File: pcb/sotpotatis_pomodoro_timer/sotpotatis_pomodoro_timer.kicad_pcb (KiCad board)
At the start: 2 copper layers, 46 parts, among them J1 GENERIC_PWR_IN, J2 USB_C_PWR_IN, SW1 RIGHT_BTN, SW2 PRESET_1_BTN, SW3 PRESET_2_BTN, SW4 PRESET_3_BTN, SW5 LEFT_BTN, SW6 PWR_SWITCH, U1 ATtiny84A-P

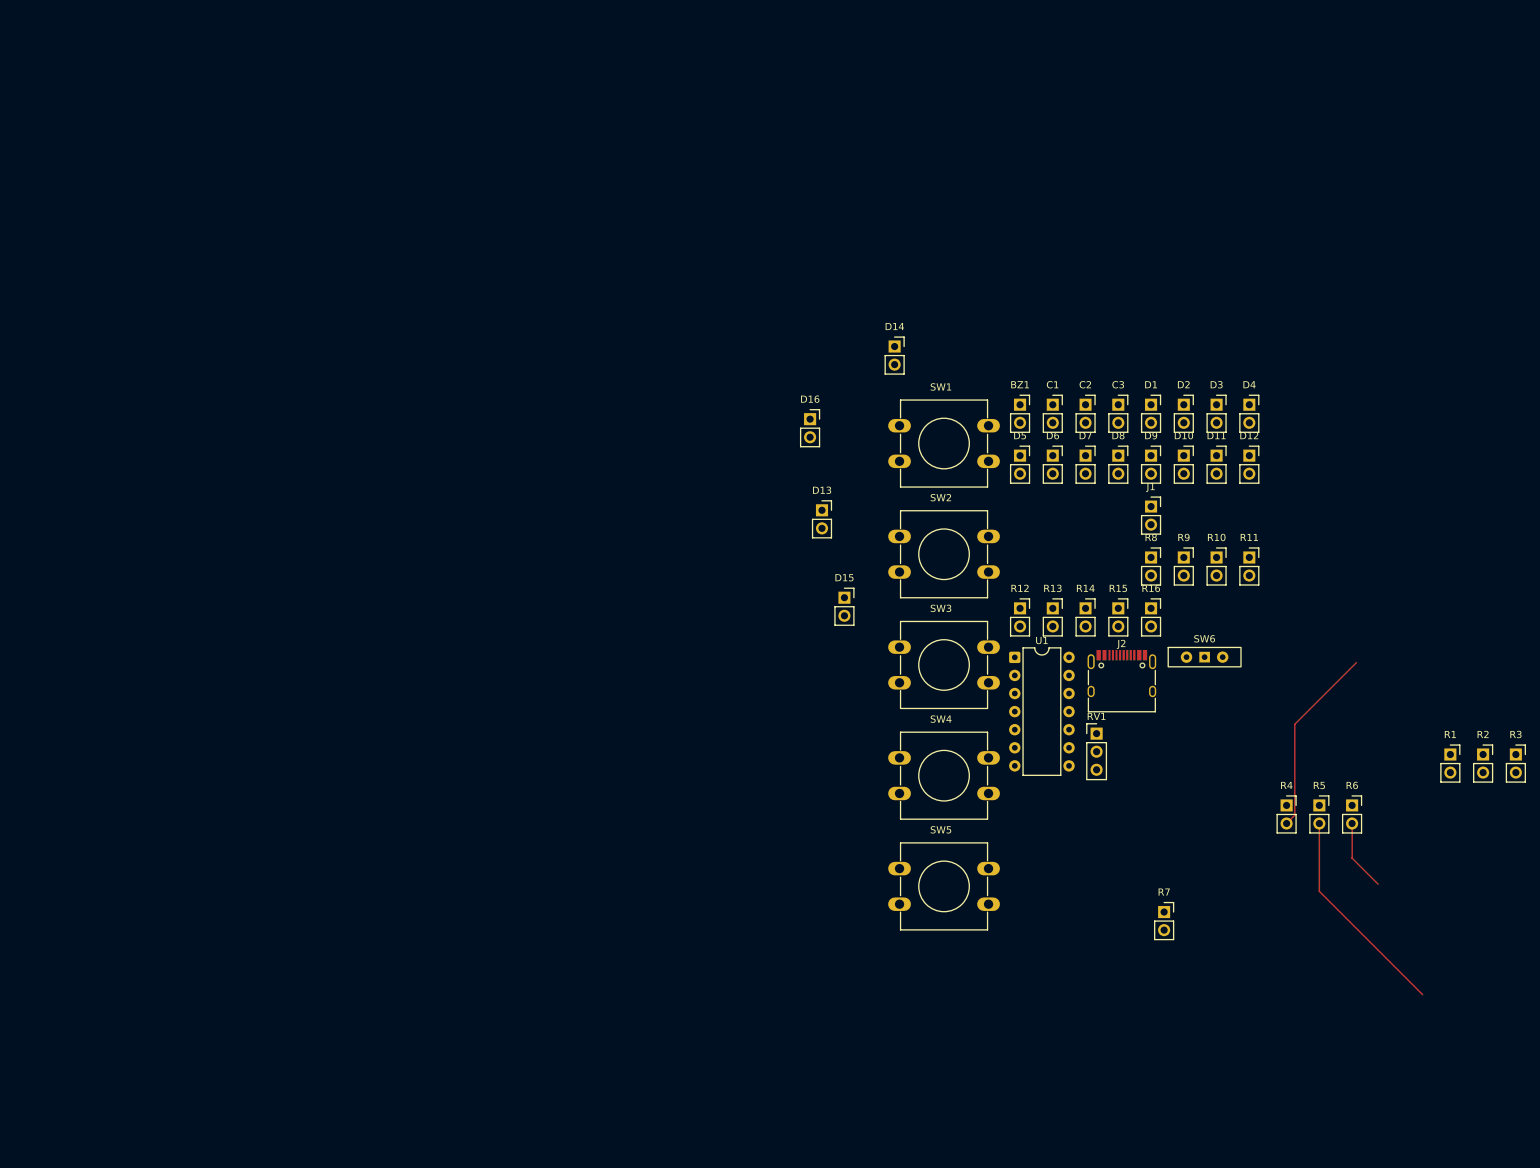
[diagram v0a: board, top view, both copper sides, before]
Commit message: add: Fix footprints in PCB, start setting up DRC settings
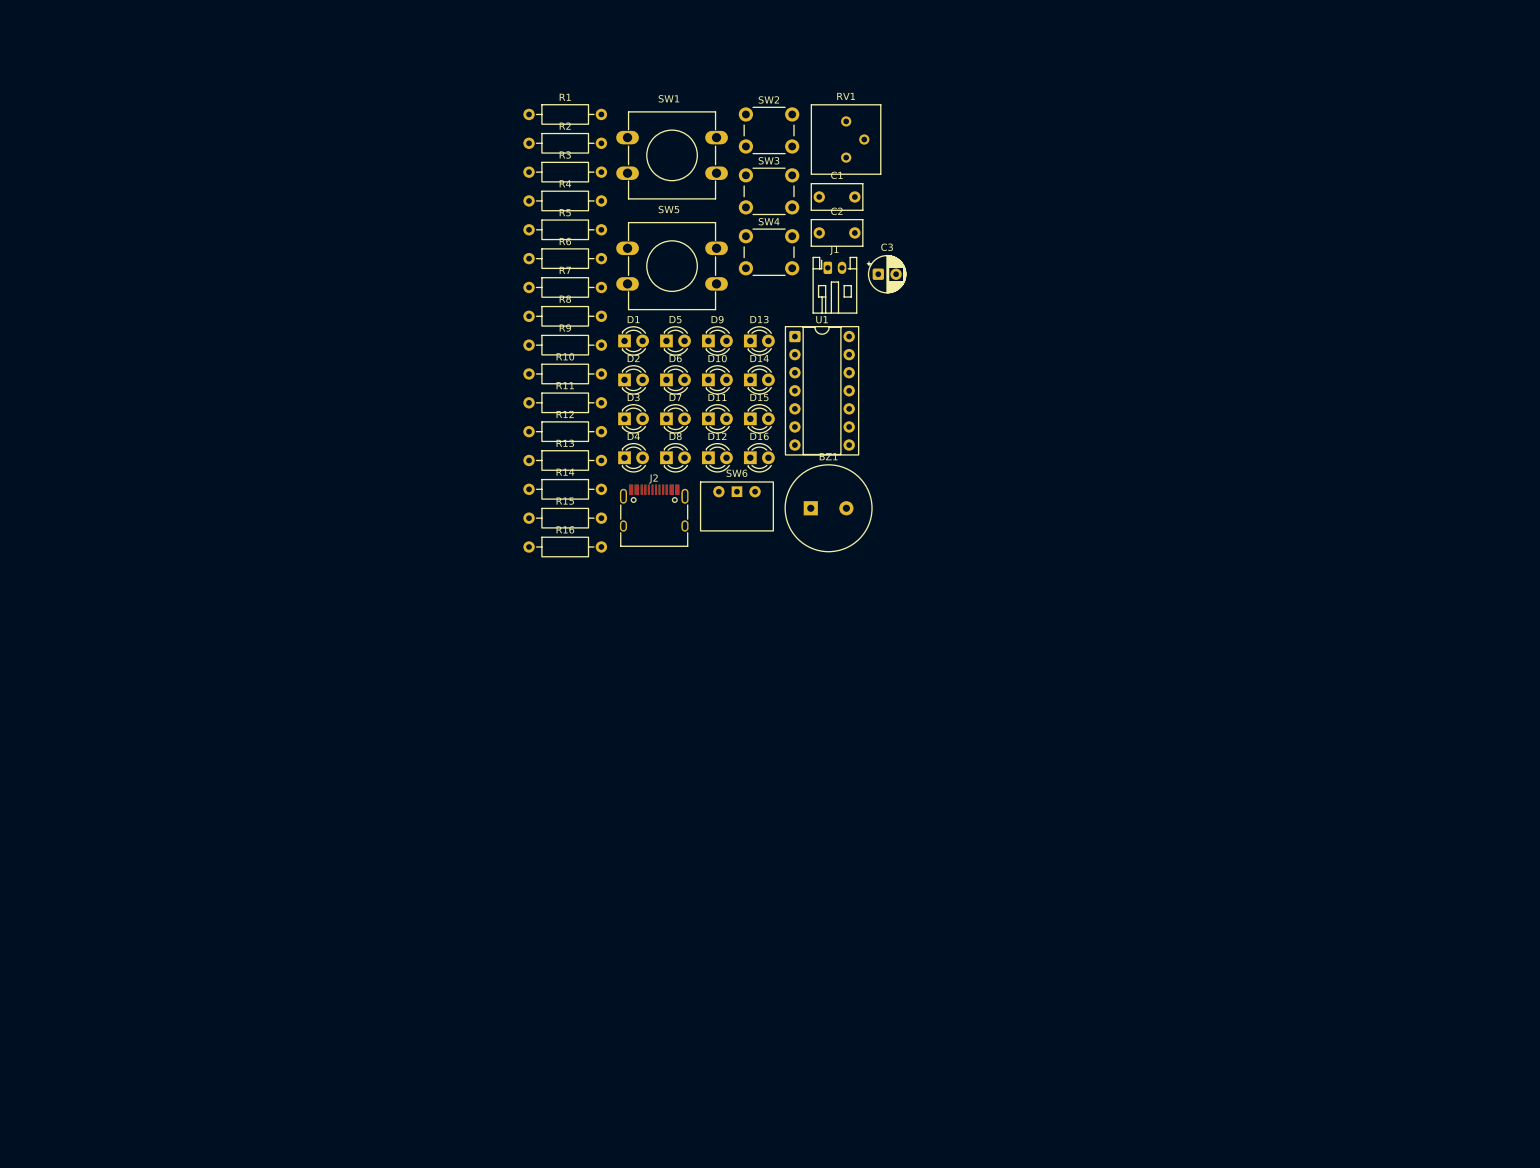
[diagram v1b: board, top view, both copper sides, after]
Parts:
- BZ1: footprint Connector_PinSocket_2.54mm:PinSocket_1x02_P2.54mm_Vertical -> custom-project-libraries:Buzzer_12x5.5RM0.6
- C1, C2: footprint Connector_PinSocket_2.54mm:PinSocket_1x02_P2.54mm_Vertical -> Capacitor_THT:C_Rect_L7.0mm_W3.5mm_P5.00mm
- C3: footprint Connector_PinSocket_2.54mm:PinSocket_1x02_P2.54mm_Vertical -> Capacitor_THT:CP_Radial_D5.0mm_P2.50mm
- D1, D10, D11, D12, D13, D14, D15, D16, D2, D3, D4, D5, D6, D7, D8, D9: footprint Connector_PinSocket_2.54mm:PinSocket_1x02_P2.54mm_Vertical -> LED_THT:LED_D3.0mm
- J1: footprint Connector_PinSocket_2.54mm:PinSocket_1x02_P2.54mm_Vertical -> Connector_JST:JST_PH_S2B-PH-K_1x02_P2.00mm_Horizontal
- R1, R10, R11, R12, R13, R14, R15, R16, R2, R3, R4, R5, R6, R7, R8, R9: footprint Connector_PinSocket_2.54mm:PinSocket_1x02_P2.54mm_Vertical -> Resistor_THT:R_Axial_DIN0207_L6.3mm_D2.5mm_P10.16mm_Horizontal
- RV1: footprint Connector_PinHeader_2.54mm:PinHeader_1x03_P2.54mm_Vertical -> Potentiometer_THT:Potentiometer_Bourns_3386P_Vertical
- SW2, SW3, SW4: footprint Button_Switch_THT:SW_PUSH-12mm -> Button_Switch_THT:SW_PUSH_6mm_H5mm
- SW6: footprint Button_Switch_THT:SW_Slide-03_Wuerth-WS-SLTV_10x2.5x6.4_P2.54mm -> custom-project-libraries:SW_Slide-03_Wuerth-WS-SLTU_10x2.5mm_P2.54mm
- U1: footprint Package_DIP:DIP-14_W7.62mm -> Package_DIP:DIP-14_W7.62mm_Socket
- moved R3 160.9 mm to (84.0, 55.4)
- moved R2 159.1 mm to (84.0, 51.4)
- moved R1 157.6 mm to (84.0, 47.3)
- moved R6 138.8 mm to (84.0, 67.6)
- moved R5 137.3 mm to (84.0, 63.5)
- moved R4 136.1 mm to (84.0, 59.5)
- moved R7 125.1 mm to (84.0, 71.6)
- moved R11 103.5 mm to (84.0, 87.8)
- moved R10 99.9 mm to (84.0, 83.8)
- moved R9 96.7 mm to (84.0, 79.7)
- moved SW5 95.1 mm to (97.8, 66.1)
- moved R8 93.7 mm to (84.0, 75.7)
- moved RV1 88.2 mm to (128.5, 53.4)
- moved D4 88.1 mm to (97.4, 95.5)
- moved R16 87.8 mm to (84.0, 108.1)
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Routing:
- net Net-(D10-A): track 30.0 -> 0.00 mm
- net Net-(D11-A): track 26.6 -> 0.00 mm
- net Net-(D13-K): track 10.0 -> 0.00 mm

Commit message: add: Finalize DRC settings, switch to 4-layer
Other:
- copper layers 2 -> 4
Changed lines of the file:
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@@
 	(generator_version "9.0")
 	(general
-		(thickness 1.6)
+		(thickness 1.586)
 		(legacy_teardrops no)
 	)
@@
 	(layers
 		(0 "F.Cu" signal)
+		(4 "In1.Cu" signal)
+		(6 "In2.Cu" signal)
 		(2 "B.Cu" signal)
 		(9 "F.Adhes" user "F.Adhesive")
@@
 			(layer "F.SilkS"
 				(type "Top Silk Screen")
+				(color "White")
 			)
 			(layer "F.Paste"
@@
 			(layer "F.Mask"
 				(type "Top Solder Mask")
+				(color "Black")
 				(thickness 0.01)
 			)
@@
 			)
 			(layer "dielectric 1"
+				(type "prepreg")
+				(thickness 0.203)
+				(material "FR4")
+				(epsilon_r 4.5)
+				(loss_tangent 0.02)
+			)
+			(layer "In1.Cu"
+				(type "copper")
+				(thickness 0.03)
+			)
+			(layer "dielectric 2"
 				(type "core")
-				(thickness 1.51)
+				(thickness 1.03)
+				(material "FR4")
+				(epsilon_r 4.5)
+				(loss_tangent 0.02)
+			)
+			(layer "In2.Cu"
+				(type "copper")
+				(thickness 0.03)
+			)
+			(layer "dielectric 3"
+				(type "prepreg")
+				(thickness 0.203)
 				(material "FR4")
 				(epsilon_r 4.5)
@@
 			(layer "B.Mask"
 				(type "Bottom Solder Mask")
+				(color "Black")
 				(thickness 0.01)
 			)
@@
 			(layer "B.SilkS"
 				(type "Bottom Silk Screen")
+				(color "White")
 			)
 			(copper_finish "None")
@@
 		)
 	)
+	(segment
+		(start 113.154 100.286)
+		(end 113.154 100.2)
+		(width 0.2)
+		(layer "F.Cu")
+		(net 11)
+	)
+	(segment
+		(start 113.154 100.2)
+		(end 113.03 100.076)
+		(width 0.2)
+		(layer "F.Cu")
+		(net 11)
+	)
 	(embedded_fonts no)

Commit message: add: Backup PCB progress. Working with placement.
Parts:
- C1, C2: footprint Capacitor_THT:C_Rect_L7.0mm_W3.5mm_P5.00mm -> Capacitor_SMD:C_1206_3216Metric_Pad1.33x1.80mm_HandSolder
- C3: footprint Capacitor_THT:CP_Radial_D5.0mm_P2.50mm -> Capacitor_SMD:C_1206_3216Metric_Pad1.33x1.80mm_HandSolder; moved to B.Cu
- D16, J1, J2, SW6: moved to B.Cu
- R1, R10, R11, R12, R2, R3, R4, R5, R6, R7, R8, R9: footprint Resistor_THT:R_Axial_DIN0207_L6.3mm_D2.5mm_P10.16mm_Horizontal -> Resistor_SMD:R_0805_2012Metric_Pad1.20x1.40mm_HandSolder
- R13: value 2.2K -> 2.2k; footprint Resistor_THT:R_Axial_DIN0207_L6.3mm_D2.5mm_P10.16mm_Horizontal -> Resistor_SMD:R_0805_2012Metric_Pad1.20x1.40mm_HandSolder; moved to B.Cu
- R14, R15, R16: footprint Resistor_THT:R_Axial_DIN0207_L6.3mm_D2.5mm_P10.16mm_Horizontal -> Resistor_SMD:R_0805_2012Metric_Pad1.20x1.40mm_HandSolder; moved to B.Cu
- SW1, SW5: footprint Button_Switch_THT:SW_PUSH-12mm -> Button_Switch_THT:SW_PUSH_6mm_H5mm
- moved R2 117.4 mm to (139.8, 154.6), turned to 90 degrees
- moved R5 117.2 mm to (157.2, 155.0), turned to 90 degrees
- moved R1 117.0 mm to (132.6, 153.7), turned to 90 degrees
- moved R3 115.8 mm to (143.8, 154.5), turned to 90 degrees
- moved R8 111.8 mm to (179.2, 134.2), turned to 90 degrees
- moved SW1 110.3 mm to (170.2, 133.8)
- moved R13 109.0 mm to (179.3, 148.7), turned to 180 degrees
- moved R6 108.6 mm to (161.1, 144.0), turned to 90 degrees
- moved R14 108.4 mm to (178.5, 153.0), turned to 90 degrees
- moved R4 107.7 mm to (136.1, 153.7), turned to 90 degrees
- moved R16 106.5 mm to (178.5, 157.2), turned to 90 degrees
- moved R9 99.9 mm to (167.8, 134.0), turned to 90 degrees
- moved SW2 97.0 mm to (158.7, 133.6)
- moved R15 95.1 mm to (165.5, 153.0), turned to 90 degrees
- moved J1 93.5 mm to (163.8, 154.3), turned to 180 degrees
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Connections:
- C3 pad 1: VCC -> +5V
- J1 pad 2: Net-(J1-Pin_2) -> +5V
- J2 pad A4: Net-(J1-Pin_2) -> +5V
- J2 pad A9: Net-(J1-Pin_2) -> +5V
- J2 pad B4: Net-(J1-Pin_2) -> +5V
- J2 pad B9: Net-(J1-Pin_2) -> +5V
- SW6 pad 1: Net-(J1-Pin_2) -> +5V
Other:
- board outline added: 88 x 62.7 mm
- board text added: "1"
- board text added: "10M"
- board text added: "15M"
- board text added: "1M"
- board text added: "20M"
- board text added: "25M"
- board text added: "30M"
- board text added: "3M"
- board text added: "45M"
- board text added: "5M"
- board text added: "60M"
- board text added: "75M"
- board text added: "90M"
- board text added: "BREAK"
- board text added: "PRESETS"
- board text added: "PUT ICONS HERE AND NEWLINES?"
- board text added: "REPETITIONS"
- board text added: "VOLUME"
- board text added: "WORK"

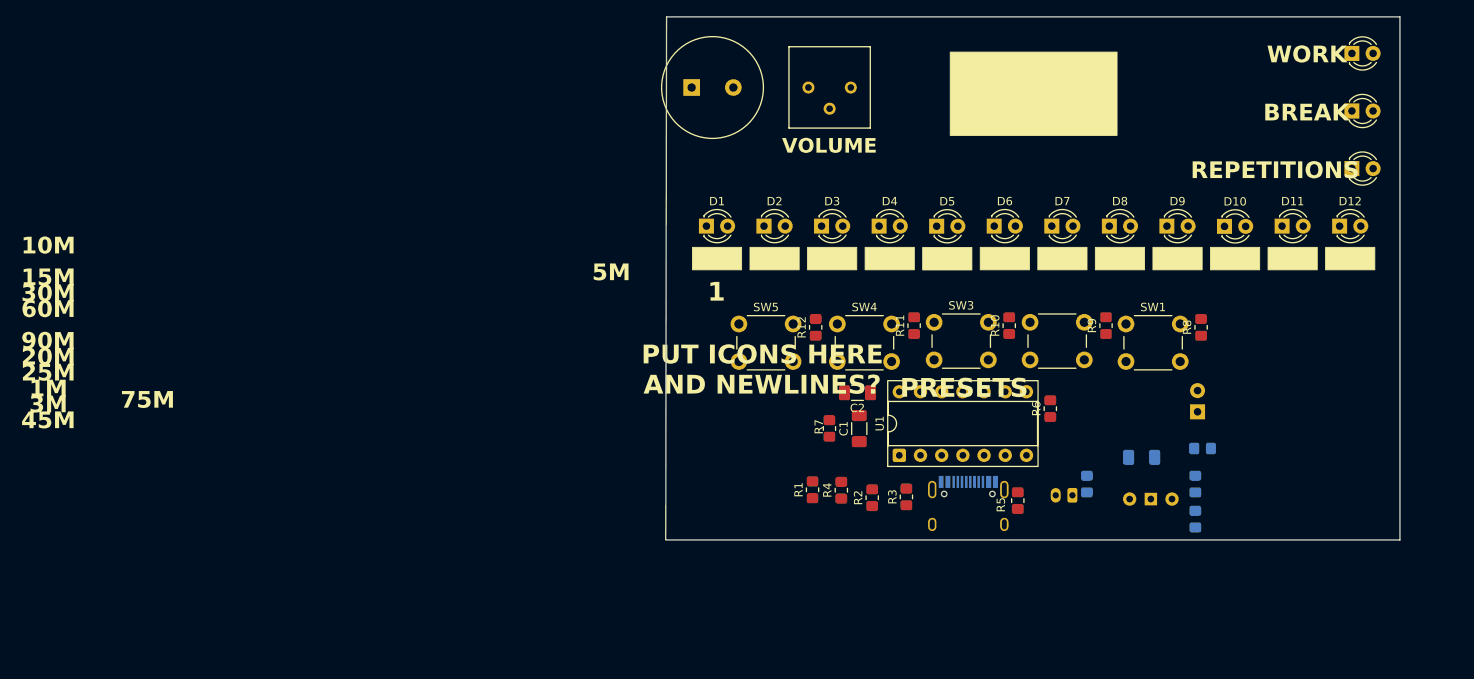
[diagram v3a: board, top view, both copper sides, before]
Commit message: add: Layout variant 1 of PCB
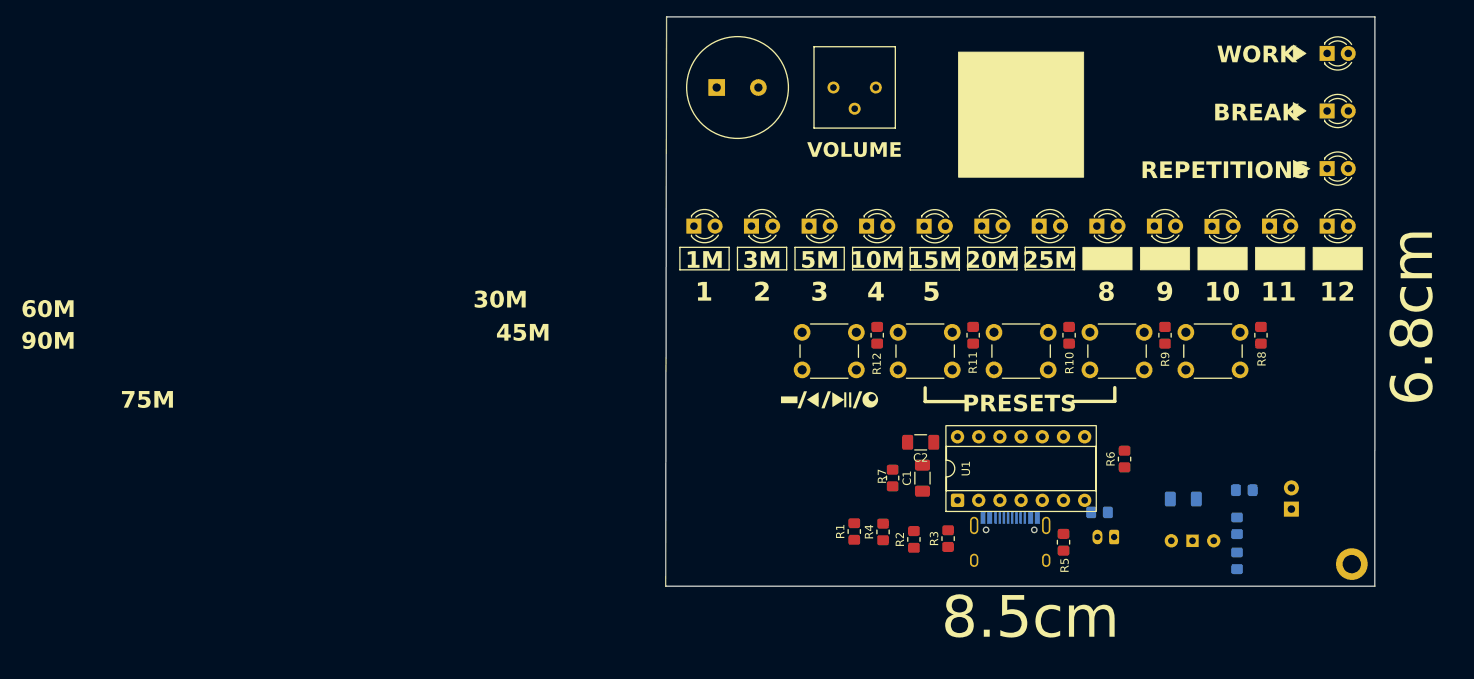
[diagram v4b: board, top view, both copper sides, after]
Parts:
- added G***: LOGO, LOGO, F.Cu at (134.6, 142.9)
- added REF**: MountingHole_2.2mm_M2_DIN965_Pad, MountingHole:MountingHole_2.2mm_M2_DIN965_Pad, F.Cu at (197.2, 162.6)
- moved D16 16.2 mm to (190.0, 156.0)
- moved R6 10.8 mm to (170.0, 150.0)
- moved C1 9.62 mm to (145.8, 152.3)
- moved R7 9.62 mm to (142.2, 152.3)
- moved C2 9.62 mm to (145.6, 148.0)
- moved U1 8.82 mm to (150.0, 154.9)
- moved SW5 7.64 mm to (131.3, 134.8)
- moved R12 7.44 mm to (140.3, 135.2)
- moved R5 7.41 mm to (162.7, 160.0)
- moved SW4 7.34 mm to (142.8, 134.8)
- moved SW2 7.27 mm to (165.8, 134.8)
- moved SW3 7.27 mm to (154.3, 134.8)
- moved R10 7.27 mm to (163.3, 135.2)
- moved SW1 7.24 mm to (177.3, 134.8)
- moved R8 7.24 mm to (186.3, 135.2)
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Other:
- board size 88 x 62.7 mm -> 85 x 68.2 mm
- board text added: "10"
- board text added: "11"
- board text added: "12"
- board text added: "2"
- board text added: "3"
- board text added: "4"
- board text added: "5"
- board text added: "6.8cm"
- board text added: "8"
- board text added: "8.5cm"
- board text added: "9"
- board text added: "Alignment for LED number text"
- board text added: "Board center"

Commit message: add: Layout variant 1 of PCB
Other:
- board text added: "VARIANT 1"
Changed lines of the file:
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@@
+		)
+	)
+	(gr_text "VARIANT 1"
+		(at 137.625 93.949 0)
+		(layer "F.SilkS")
+		(effects
+			(font
+				(size 5 5)
+				(thickness 0.15)
+			)
+			(justify left bottom)
 		)
 	)
